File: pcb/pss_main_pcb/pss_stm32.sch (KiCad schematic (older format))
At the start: 24 parts, among them J5 STM32_Prog, SW1 Hot Air Gun Input, SW2 Soldering Iron Input, SW3 SW_Push, U5 STM32F030K6Tx

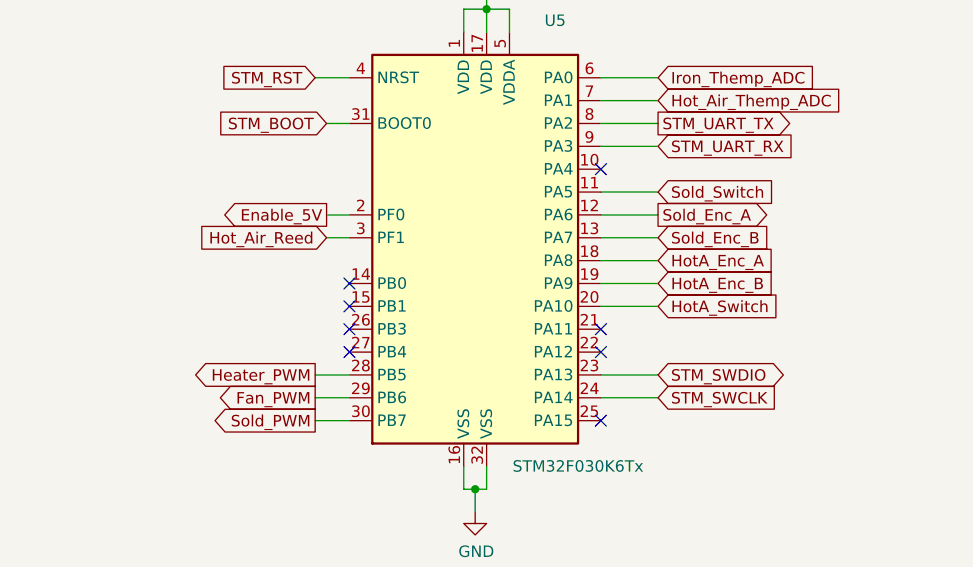
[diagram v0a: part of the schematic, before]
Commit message: Add encoders routes
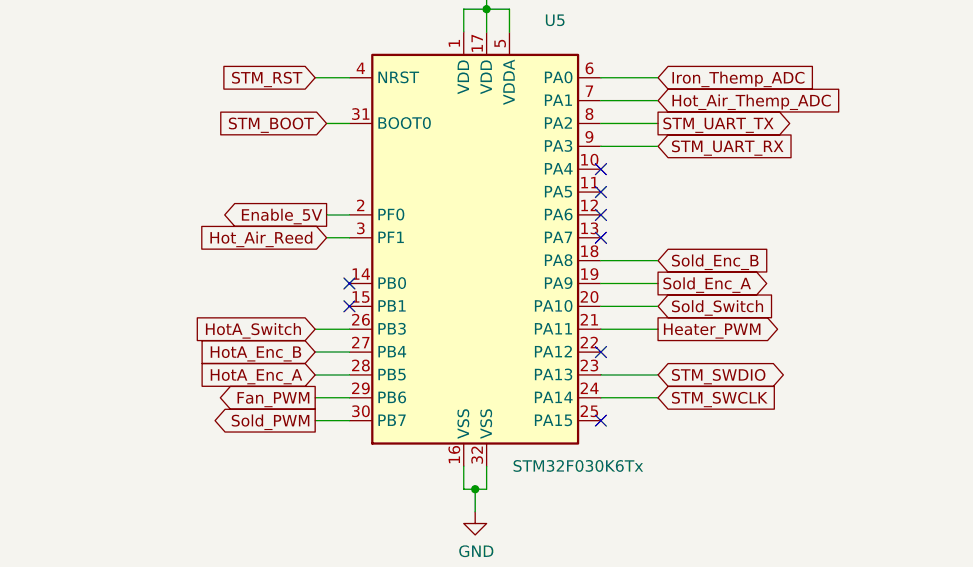
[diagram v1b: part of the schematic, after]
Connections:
- net Heater_PWM: now also U5.21 (PA11); no longer U5.28 (PB5)
- net HotA_Enc_A: now also U5.28 (PB5); no longer U5.18 (PA8)
- net HotA_Enc_B: now also U5.27 (PB4); no longer U5.19 (PA9)
- net HotA_Switch: now also U5.26 (PB3); no longer U5.20 (PA10)
- net Sold_Enc_A: now also U5.19 (PA9); no longer U5.12 (PA6)
- net Sold_Enc_B: now also U5.18 (PA8); no longer U5.13 (PA7)
- net Sold_Switch: now also U5.20 (PA10); no longer U5.11 (PA5)
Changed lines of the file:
@@
 Wire Wire Line
 	6300 3850 6550 3850
-Text GLabel 6550 4050 2    50   Input ~ 0
+Text GLabel 6550 4550 2    50   Input ~ 0
 Sold_Switch
-Wire Wire Line
-	6300 4050 6550 4050
 NoConn ~ 6300 3950
-Text GLabel 6550 4150 2    50   Output ~ 0
+Text GLabel 6550 4450 2    50   Output ~ 0
 Sold_Enc_A
-Text GLabel 6550 4250 2    50   Input ~ 0
+Text GLabel 6550 4350 2    50   Input ~ 0
 Sold_Enc_B
-Wire Wire Line
-	6300 4150 6550 4150
-Wire Wire Line
-	6550 4250 6300 4250
 $Comp
 L Device:R R22
@@
 Wire Wire Line
 	950  7300 1450 7300
-Text GLabel 6550 4350 2    50   Input ~ 0
+Text GLabel 5050 4850 0    50   Input ~ 0
 HotA_Enc_A
 Wire Wire Line
 	6300 4350 6550 4350
-Text GLabel 6550 4450 2    50   Input ~ 0
+Text GLabel 5050 4750 0    50   Input ~ 0
 HotA_Enc_B
 Wire Wire Line
 	6550 4450 6300 4450
-Text GLabel 6550 4550 2    50   Input ~ 0
+Text GLabel 5050 4650 0    50   Input ~ 0
 HotA_Switch
 Wire Wire Line
@@
 Wire Wire Line
 	5200 5050 5050 5050
-Text GLabel 5050 4850 0    50   Output ~ 0
+Text GLabel 6550 4650 2    50   Output ~ 0
 Heater_PWM
 Text GLabel 5100 4150 0    50   Output ~ 0
@@
 NoConn ~ 5200 4450
 NoConn ~ 5200 4550
-NoConn ~ 5200 4650
-NoConn ~ 5200 4750
 NoConn ~ 6300 4750
 $Comp
@@
 NoConn ~ 6300 5050
 Wire Wire Line
+	5200 4950 5050 4950
+Wire Wire Line
+	6550 4650 6300 4650
+Wire Wire Line
+	5050 4650 5200 4650
+Wire Wire Line
+	5050 4750 5200 4750
+Wire Wire Line
 	5050 4850 5200 4850
-Wire Wire Line
-	5200 4950 5050 4950
-NoConn ~ 6300 4650
+NoConn ~ 6300 4250
+NoConn ~ 6300 4150
+NoConn ~ 6300 4050
 $EndSCHEMATC

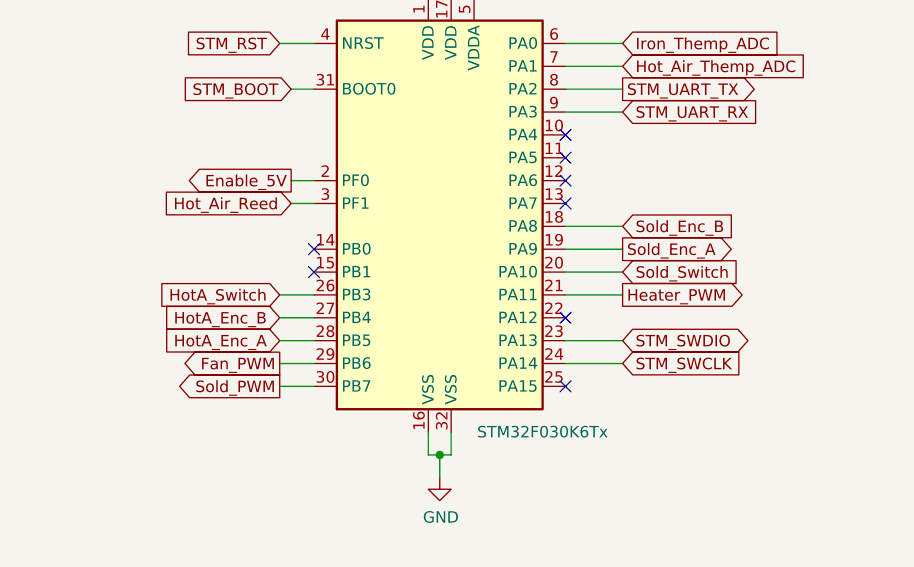
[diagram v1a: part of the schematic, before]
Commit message: Add 3D models and totaly redesign PCB
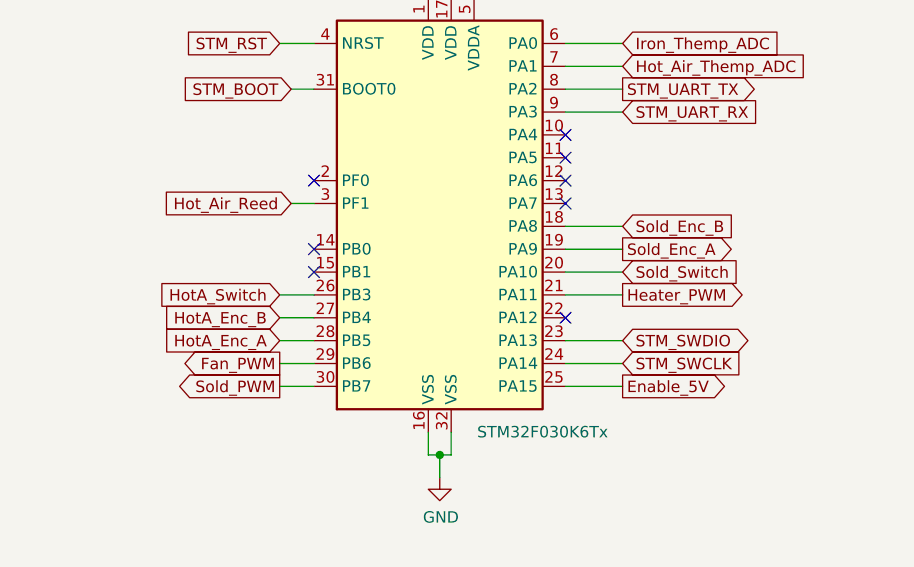
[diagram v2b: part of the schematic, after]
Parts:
- SW1, SW2: footprint Rotary_Encoder:RotaryEncoder_Alps_EC11E-Switch_Vertical_H20mm -> encoders:RotaryEncoder_Alps_EC11E-Switch_Vertical_H20mm
- SW3: footprint Button_Switch_SMD:SW_SPST_B3S-1000 -> buttons:SW_SPST_B3S-1000
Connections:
- net Enable_5V: now also U5.25 (PA15); no longer U5.2 (PF0)
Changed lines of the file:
@@
 F 0 "SW3" H 3700 1385 50  0000 C CNN
 F 1 "SW_Push" H 3700 1294 50  0000 C CNN
-F 2 "Button_Switch_SMD:SW_SPST_B3S-1000" H 3700 1300 50  0001 C CNN
+F 2 "buttons:SW_SPST_B3S-1000" H 3700 1300 50  0001 C CNN
 F 3 "~" H 3700 1300 50  0001 C CNN
 	1    3700 1100
@@
 F 0 "SW2" H 1800 6467 50  0000 C CNN
 F 1 "Soldering Iron Input" H 1800 6376 50  0000 C CNN
-F 2 "Rotary_Encoder:RotaryEncoder_Alps_EC11E-Switch_Vertical_H20mm" H 1650 6260 50  0001 C CNN
+F 2 "encoders:RotaryEncoder_Alps_EC11E-Switch_Vertical_H20mm" H 1650 6260 50  0001 C CNN
 F 3 "~" H 1800 6360 50  0001 C CNN
 	1    1800 6100
@@
 F 0 "SW1" H 1750 7667 50  0000 C CNN
 F 1 "Hot Air Gun Input" H 1750 7576 50  0000 C CNN
-F 2 "Rotary_Encoder:RotaryEncoder_Alps_EC11E-Switch_Vertical_H20mm" H 1600 7460 50  0001 C CNN
+F 2 "encoders:RotaryEncoder_Alps_EC11E-Switch_Vertical_H20mm" H 1600 7460 50  0001 C CNN
 F 3 "~" H 1750 7560 50  0001 C CNN
 	1    1750 7300
@@
 Text GLabel 6550 4650 2    50   Output ~ 0
 Heater_PWM
-Text GLabel 5100 4150 0    50   Output ~ 0
+Text GLabel 6550 5050 2    50   Output ~ 0
 Enable_5V
-Wire Wire Line
-	5200 4150 5100 4150
 NoConn ~ 5200 4450
 NoConn ~ 5200 4550
@@
 Wire Wire Line
 	5200 4250 5100 4250
-NoConn ~ 6300 5050
 Wire Wire Line
 	5200 4950 5050 4950
@@
 NoConn ~ 6300 4150
 NoConn ~ 6300 4050
+Wire Wire Line
+	6300 5050 6550 5050
+NoConn ~ 5200 4150
 $EndSCHEMATC
